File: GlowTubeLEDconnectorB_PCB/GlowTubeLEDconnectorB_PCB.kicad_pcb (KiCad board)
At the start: 2 copper layers, 39.4 x 39.4 mm, 2 parts

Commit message: added readme to pcb files
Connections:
- net LED1 DATA OUT renamed Net-(LED2-Pad2)
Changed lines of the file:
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@@
   )
   (net 0 "")
-  (net 1 "LED1 DATA OUT")
+  (net 1 "Net-(LED2-Pad2)")
   (footprint "Connector:LED strip connector pad" (layer "F.Cu")
     (at 86.369 67.17 -90)
     (property "Sheetfile" "GlowTubeLEDconnectorB_PCB.kicad_sch")
     (property "Sheetname" "")
-    (attr exclude_from_pos_files exclude_from_bom)
+    (attr exclude_from_pos_files)
     (fp_text reference "LED1" (at 0.1524 -3.5306 -90 unlocked) (layer "F.SilkS") hide
       (effects (font (size 1 1) (thickness 0.15)))
@@
     (fp_rect (start -5 -12.1412) (end 5 -2.159) (layer "F.Fab") (width 0.12) (fill none))
     (pad "2" smd rect (at 0.0381 -0.381 270) (size 2 3.5) (layers "F.Cu" "F.Mask")
-      (net 1 "LED1 DATA OUT") (pinfunction "Data") (pintype "bidirectional"))
+      (net 1 "Net-(LED2-Pad2)") (pinfunction "Data") (pintype "bidirectional"))
   )
   (footprint "Connector:LED strip connector pad" (layer "F.Cu")
@@
     (property "Sheetfile" "GlowTubeLEDconnectorB_PCB.kicad_sch")
     (property "Sheetname" "")
-    (attr exclude_from_pos_files exclude_from_bom)
+    (attr exclude_from_pos_files)
     (fp_text reference "LED2" (at 0.1524 -3.5306 90 unlocked) (layer "F.SilkS") hide
       (effects (font (size 1 1) (thickness 0.15)))
@@
     (fp_rect (start -5 -12.1412) (end 5 -2.159) (layer "F.Fab") (width 0.12) (fill none))
     (pad "2" smd rect (at 0.0381 -0.381 90) (size 2 3.5) (layers "F.Cu" "F.Mask")
-      (net 1 "LED1 DATA OUT") (pinfunction "Data") (pintype "bidirectional"))
+      (net 1 "Net-(LED2-Pad2)") (pinfunction "Data") (pintype "bidirectional"))
   )
   (gr_arc (start 89.054214 72.48) (mid 88.842082 72.392132) (end 88.754214 72.18) (layer "Edge.Cuts") (width 0.1))

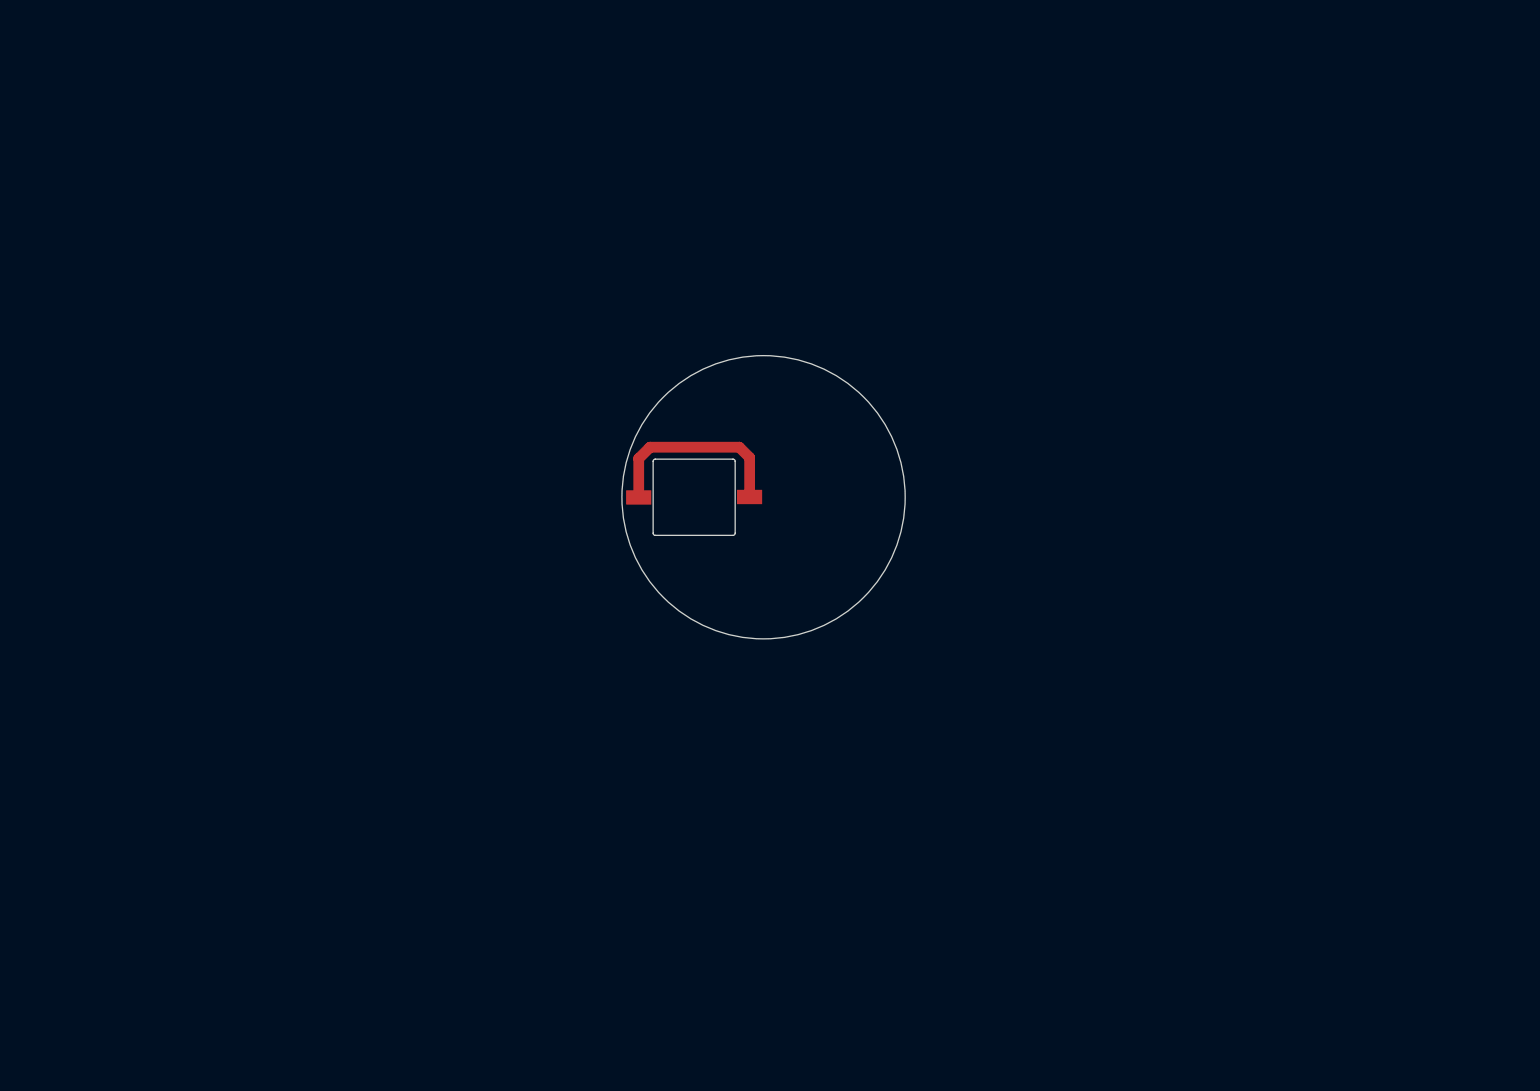
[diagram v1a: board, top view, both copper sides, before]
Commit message: redesigned GlowTube PCBs
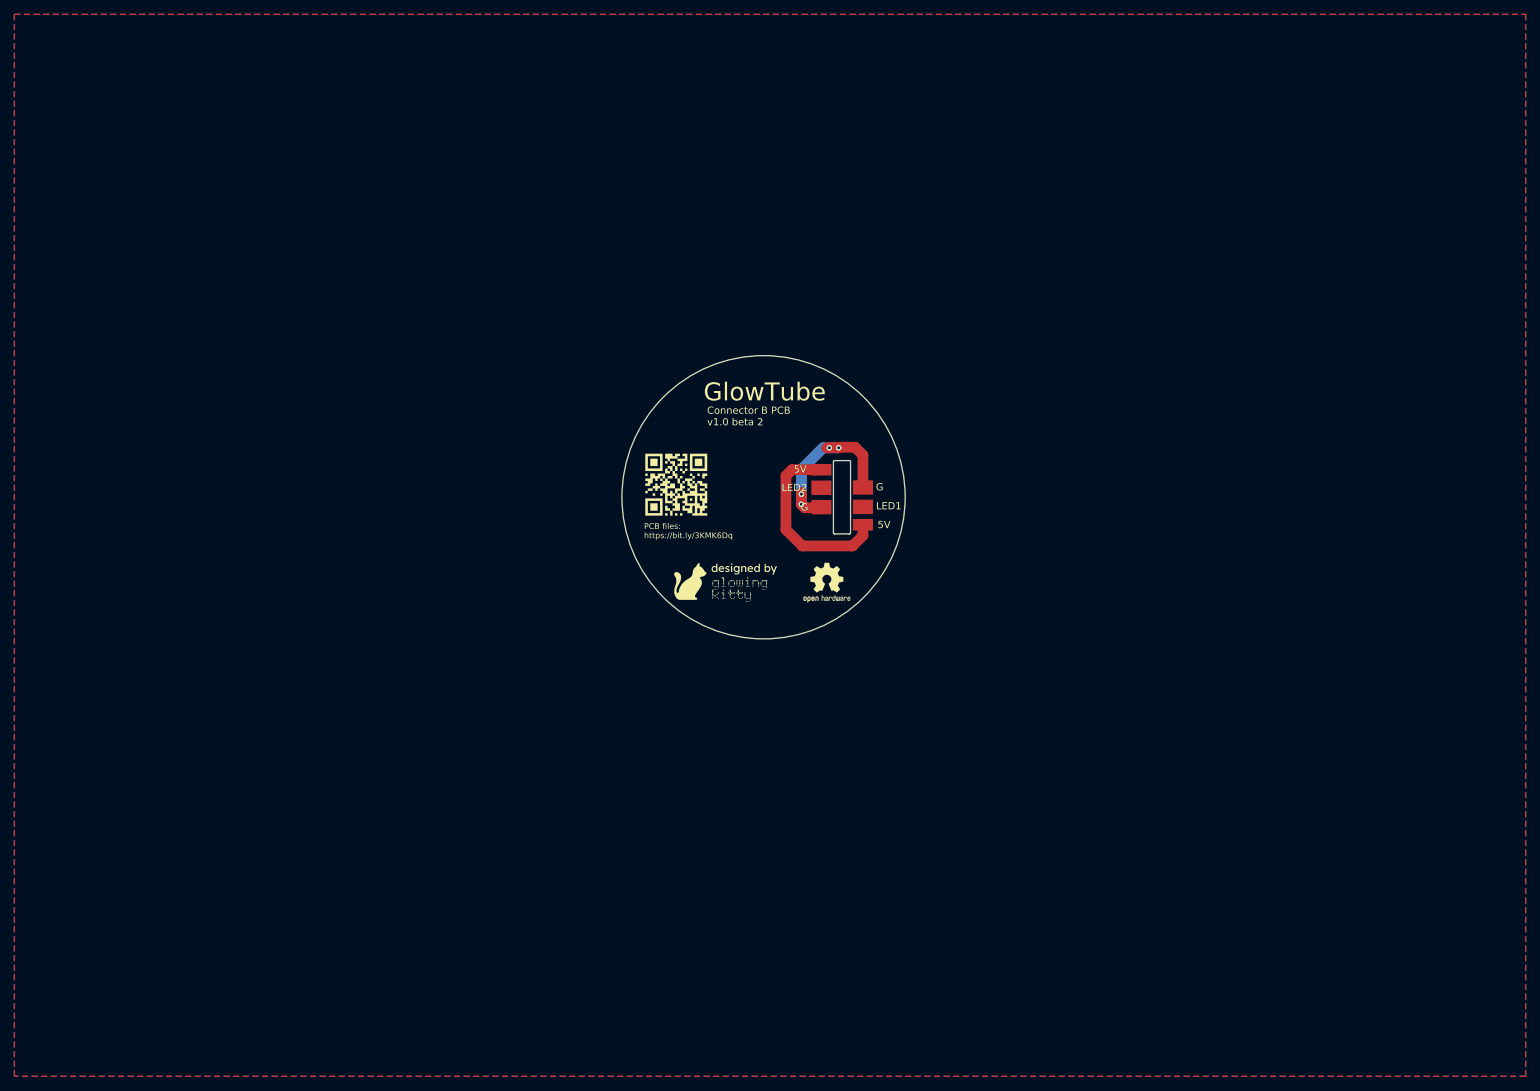
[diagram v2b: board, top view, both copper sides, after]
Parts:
- removed LED1, LED2: LED_strip_contact_pads, Connector:LED strip connector pad
- added OSHW logo: OSHW-Logo2_7.3x6mm_SilkScreen, Symbol:OSHW-Logo2_7.3x6mm_SilkScreen, F.Cu at (112.9, 79.1)
- added U1: Contact pads, myparts:LED strip connector 4pad small, F.Cu at (117.9, 67.2)
- added U2: Contact pads, myparts:LED strip connector 4pad small, F.Cu at (112.1, 67.2)
- added designedby: LOGO, LOGO, F.Cu at (98.9, 78.9)
- added qrcode: LOGO, LOGO, F.Cu at (92.0, 65.4)
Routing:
- net Net-(LED2-Pad2): track 27.6 -> 0.00 mm
- net +5V: track 0.00 -> 26.5 mm
- net GND: track 0.00 -> 26.0 mm, vias 0 -> 4
- added copper zone on B.Cu, net GND
- added copper zone on F.Cu, net GND
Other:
- outline, holes or cut-outs redrawn
- board text added: "5V"
- board text added: "Connector B PCB v1.0 beta 2"
- board text added: "G"
- board text added: "GlowTube"
- board text added: "LED1"
- board text added: "LED2"
- board text added: "PCB files: https://bit.ly/3KMK6Dq"

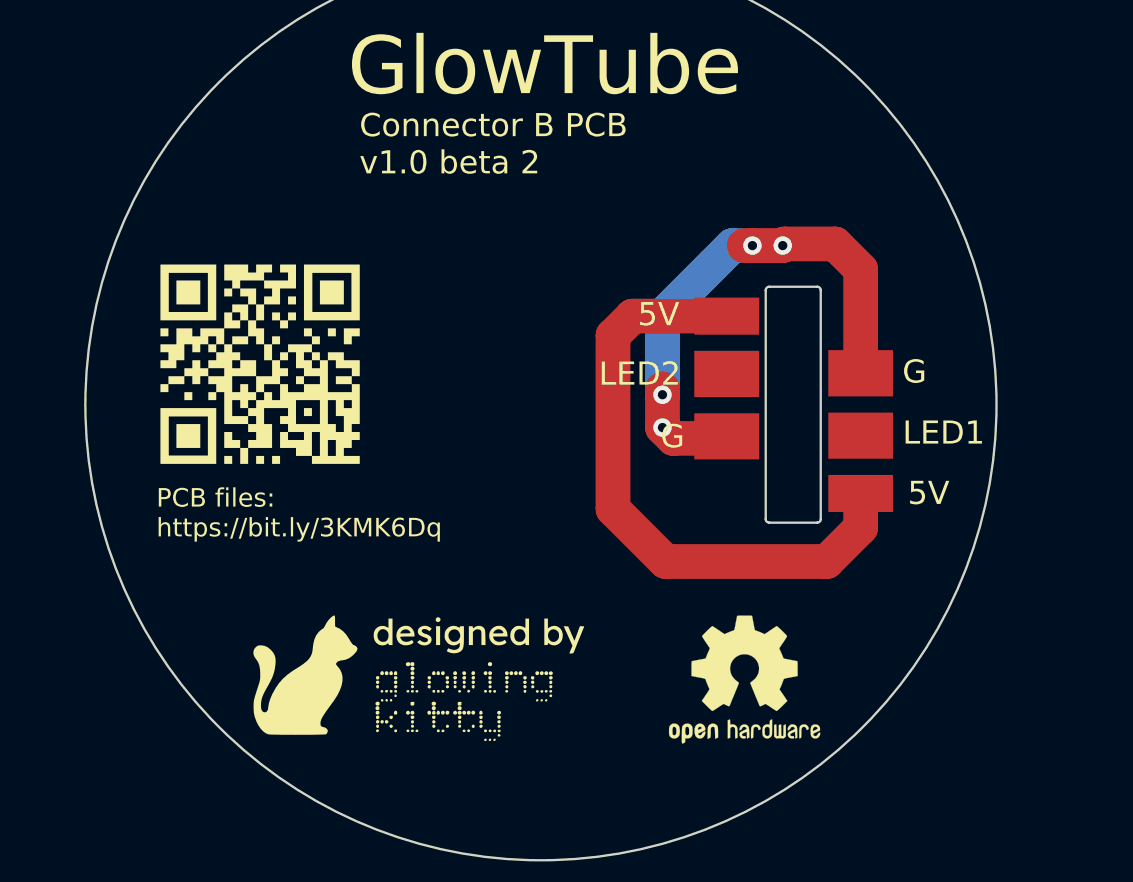
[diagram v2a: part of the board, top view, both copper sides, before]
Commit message: updated PCB designs to release candidate 1
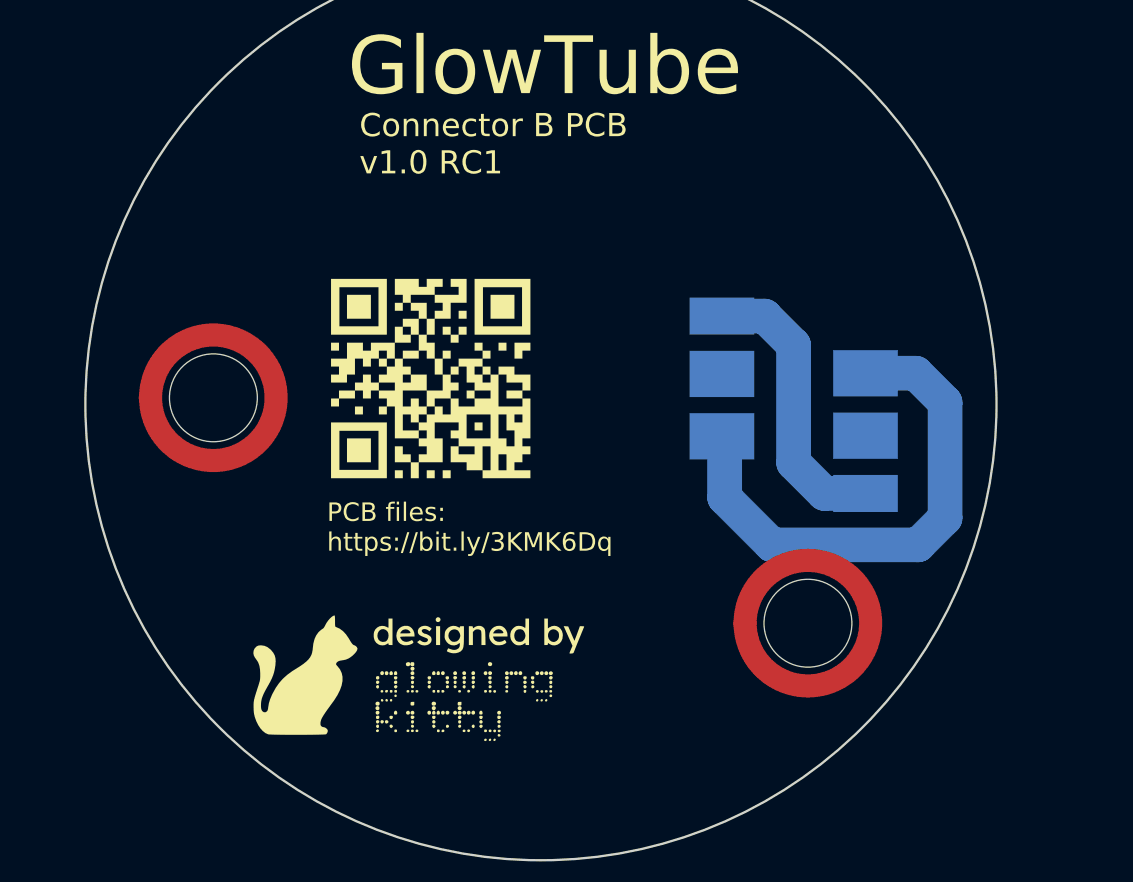
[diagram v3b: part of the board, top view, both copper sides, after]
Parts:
- removed OSHW logo: OSHW-Logo2_7.3x6mm_SilkScreen, Symbol:OSHW-Logo2_7.3x6mm_SilkScreen
- added U3: SMTSO3015CTJ, footprint:SMTSO3030CTJ, F.Cu at (115.7, 76.6)
- added U4: SMTSO3015CTJ, footprint:SMTSO3030CTJ, F.Cu at (89.9, 66.9)
- U1, U2: moved to B.Cu
- moved qrcode 7.40 mm to (99.3, 66.0)
- moved U1 0.20 mm to (118.1, 67.2)
- moved U2 0.20 mm to (111.9, 67.2)
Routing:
- net +5V: track 26.5 -> 13.2 mm
- net GND: track 26.0 -> 22.3 mm, vias 4 -> 0
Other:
- outline, holes or cut-outs redrawn
- board text added: "Connector B PCB v1.0 RC1"
- board text removed: "Connector B PCB v1.0 beta 2"

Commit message: updated pcbs
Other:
- board text added: "Connector B PCB v1.0"
- board text removed: "Connector B PCB v1.0 RC1"
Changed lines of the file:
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@@
       (effects (font (size 1 1) (thickness 0.15)))
     )
-    (pad "" np_thru_hole circle (at 0.00997 0.00254) (size 3.8 3.8) (drill 3.8) (layers F&B.Cu *.Mask))
+    (pad "" np_thru_hole circle (at 0.00997 0.00254) (size 4.3 4.3) (drill 4.3) (layers F&B.Cu *.Mask))
     (pad "1" smd custom (at -2.7178 0) (size 1 1) (layers "F.Cu" "F.Paste" "F.Mask")
       (net 6 "unconnected-(U4-Pad1)") (pinfunction "1") (pintype "unspecified")
@@
       ))
     (model "${GLOWINGKITTYPARTS}/footprint/packages3d/SMTSO3030CTJ.step"
-      (offset (xyz 0 0 0))
+      (offset (xyz 0 0 3))
       (scale (xyz 1 1 1))
-      (rotate (xyz 0 0 0))
+      (rotate (xyz 0 180 0))
     )
   )
@@
       (effects (font (size 1 1) (thickness 0.15)))
     )
-    (pad "" np_thru_hole circle (at 0.00997 0.00254) (size 3.8 3.8) (drill 3.8) (layers F&B.Cu *.Mask))
+    (pad "" np_thru_hole circle (at 0.00997 0.00254) (size 4.3 4.3) (drill 4.3) (layers F&B.Cu *.Mask))
     (pad "1" smd custom (at -2.7178 0) (size 1 1) (layers "F.Cu" "F.Paste" "F.Mask")
       (net 5 "unconnected-(U3-Pad1)") (pinfunction "1") (pintype "unspecified")
@@
       ))
     (model "${GLOWINGKITTYPARTS}/footprint/packages3d/SMTSO3030CTJ.step"
-      (offset (xyz 0 0 0))
+      (offset (xyz 0 0 3))
       (scale (xyz 1 1 1))
-      (rotate (xyz 0 0 0))
+      (rotate (xyz 0 180 0))
     )
   )
@@
     (effects (font (size 0.8 0.8) (thickness 0.15)) (justify left))
   )
-  (gr_text "Connector B PCB \nv1.0 RC1" (at 96.26 55.91) (layer "F.SilkS")
+  (gr_text "Connector B PCB \nv1.0" (at 96.26 55.91) (layer "F.SilkS")
     (effects (font (size 1 1) (thickness 0.15)) (justify left))
   )
@@
   (segment (start 113.790734 63.350734) (end 111.5388 63.350734) (width 1.5) (layer "B.Cu") (net 1))
   (segment (start 115.04 64.6) (end 113.790734 63.350734) (width 1.5) (layer "B.Cu") (net 1))
-  (segment (start 121.59 72.077356) (end 120.427356 73.24) (width 1.5) (layer "B.Cu") (net 3))
-  (segment (start 112.06 69.070466) (end 111.5388 68.549266) (width 1.5) (layer "B.Cu") (net 3))
-  (segment (start 114.1 73.24) (end 112.06 71.2) (width 1.5) (layer "B.Cu") (net 3))
-  (segment (start 120.329802 65.819802) (end 121.59 67.08) (width 1.5) (layer "B.Cu") (net 3))
-  (segment (start 112.06 71.2) (end 112.06 69.070466) (width 1.5) (layer "B.Cu") (net 3))
   (segment (start 120.427356 73.24) (end 114.1 73.24) (width 1.5) (layer "B.Cu") (net 3))
+  (segment (start 120.329802 65.819802) (end 121.59 67.08) (width 1.5) (layer "B.Cu") (net 3))
+  (segment (start 112.06 69.070466) (end 111.5388 68.549266) (width 1.5) (layer "B.Cu") (net 3))
+  (segment (start 121.59 72.077356) (end 120.427356 73.24) (width 1.5) (layer "B.Cu") (net 3))
   (segment (start 121.59 67.08) (end 121.59 72.077356) (width 1.5) (layer "B.Cu") (net 3))
+  (segment (start 112.06 71.2) (end 112.06 69.070466) (width 1.5) (layer "B.Cu") (net 3))
   (segment (start 118.55 65.819802) (end 120.329802 65.819802) (width 1.5) (layer "B.Cu") (net 3))
+  (segment (start 114.1 73.24) (end 112.06 71.2) (width 1.5) (layer "B.Cu") (net 3))
   (zone (net 3) (net_name "GND") (layers F&B.Cu) (hatch edge 0.508)
     (connect_pads (clearance 0.508))
